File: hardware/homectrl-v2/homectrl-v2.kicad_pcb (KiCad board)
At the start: 4 copper layers, 64 x 70.5 mm, 127 parts, among them J1 Barrel_Jack, J2 PUMP1_CONN, J3 PUMP2_CONN, J4 STEP_CONN, J5 USB_C_CONN, J6 SMS1_CONN, J7 ALS_CONN, J8 FSW1_CONN, Q1 AO3407A, Q2 2N7002, Q3 AO3400A, Q4 AO3400A, SW1 S3_RESET_SW, SW2 S3_BOOT_SW, U1 TPS5405DR, U2 MCP1826S, U3 DMP4065S-7, U4 ESP32-S3-WROOM-1, U5 TMC2209, U7 TPD4E001DRLR, U8 TPD2E001DRLR, U9 SI2347DS-T1-GE3

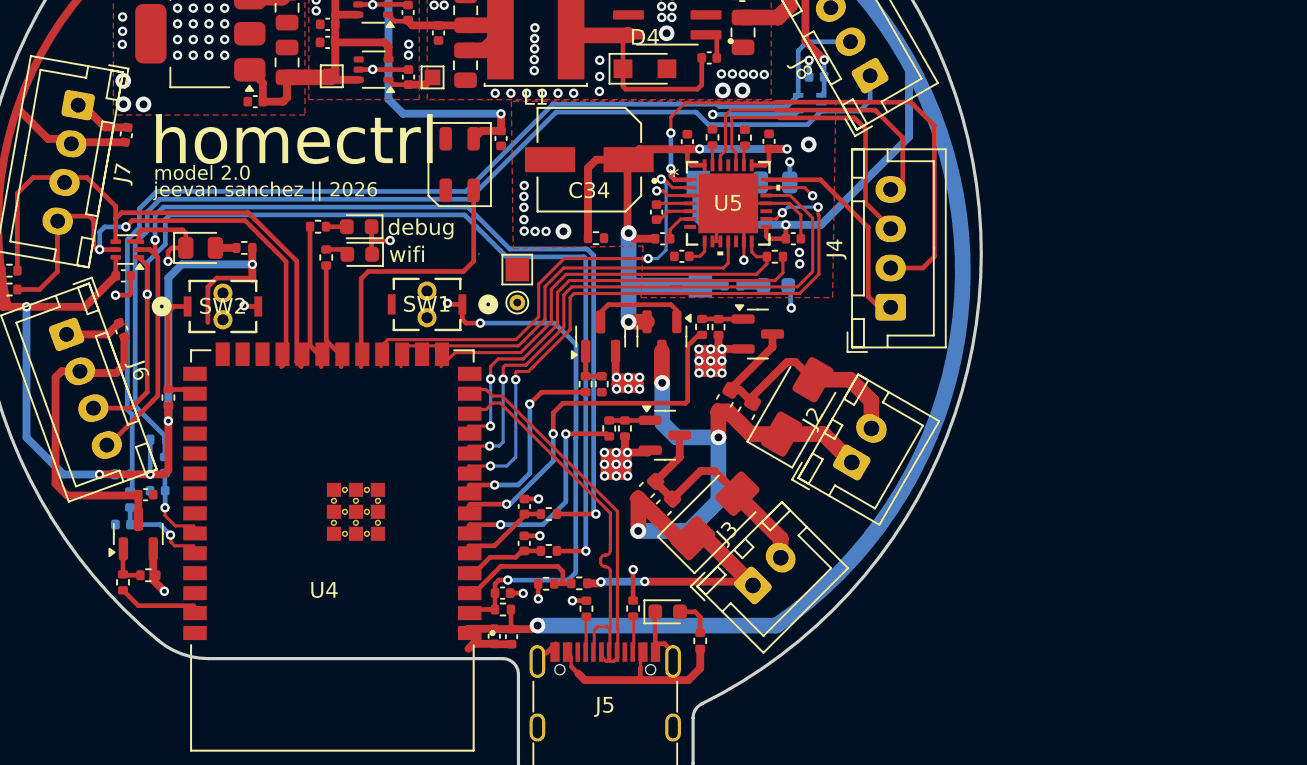
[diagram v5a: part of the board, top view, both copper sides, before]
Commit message: reroute esp pins
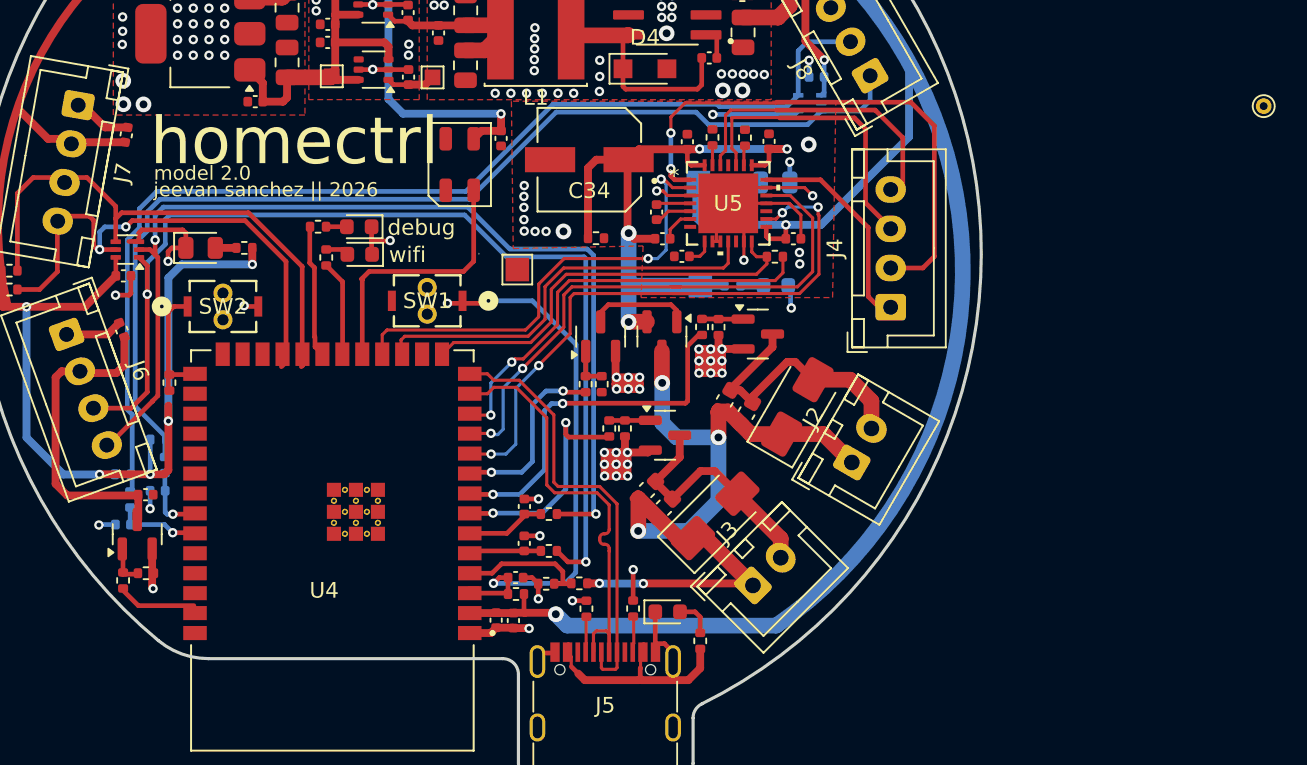
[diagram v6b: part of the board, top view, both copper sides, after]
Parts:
- moved TP3 49.2 mm to (175.5, 57.4)
- moved R9 1.29 mm to (127.9, 88.5)
- moved C17 1.29 mm to (127.8, 87.5)
- moved C16 1.03 mm to (127.7, 90.2)
- moved C14 1.03 mm to (126.6, 90.2)
- moved R14 0.95 mm to (105.8, 75.0)
- moved SW1 0.23 mm to (124.5, 69.8)
- moved R33 0.20 mm to (104.3, 87.2)
- moved R36 0.12 mm to (102.8, 87.7)
- moved Q1 0.07 mm to (103.7, 84.7)
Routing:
- net +3V3: track 198.5 -> 191.8 mm
- net USB_N: track 23.2 -> 28.2 mm
- net USB_P: track 24.1 -> 27.8 mm
- net GND: track 122.4 -> 125.7 mm, vias 152 -> 154
- net MTR_DIR: track 38.1 -> 36.5 mm
- net S3_EN: track 33.2 -> 34.7 mm
- net S3_RXD: track 28.7 -> 27.3 mm
- net MTR_STEP: track 40.9 -> 39.6 mm
- net Net-(J6-Pin_3): track 66.4 -> 67.4 mm
- net RGB_DATA: track 17.8 -> 16.9 mm
- net DBG_LED: track 9.22 -> 8.47 mm
- net WIFI_LED: track 6.84 -> 6.09 mm
- net SMS1_DATA: track 5.09 -> 4.38 mm
- net STEP_DIAG: track 26.8 -> 26.1 mm
- net VPMP_EN: track 17.4 -> 16.8 mm
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
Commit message: wrapping up layout & routing
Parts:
- removed the D8 at (107.8, 66.5)
- removed the R13 at (110.6, 66.5)
- removed TP13: 3V3_TP_DRILL, TestPoint:TestPoint_THTPad_D1.0mm_Drill0.5mm
- removed TP7: VBATT_TP_DRILL, TestPoint:TestPoint_THTPad_D1.0mm_Drill0.5mm
- added BZ1: CMT-0525-75-SMT-TR, CMT_0525_75_SMT_TR:XDCR_CMT-0525-75-SMT-TR, B.Cu at (118.8, 70.2)
- added C21: 0.1uF, Capacitor_SMD:C_0402_1005Metric, B.Cu at (113.2, 73.0)
- added D10: ON_LED, LED_SMD:LED_0603_1608Metric, F.Cu at (107.7, 66.4)
- added D13: BAT54J, Diode_SMD:D_SOD-323F, B.Cu at (115.1, 71.9)
- added Q5: AO3400A, Package_TO_SOT_SMD:SOT-23, B.Cu at (113.1, 68.3)
- added R15: 330, Resistor_SMD:R_0402_1005Metric, F.Cu at (110.5, 66.5)
- added R16: 200, Resistor_SMD:R_0402_1005Metric, B.Cu at (113.1, 71.8)
- added R19: 10k, Resistor_SMD:R_0402_1005Metric, B.Cu at (113.1, 70.8)
- added TP2: 3V3_TP_PAD, TestPoint:TestPoint_Pad_1.5x1.5mm, F.Cu at (108.4, 46.7)
- D2: footprint Diode_SMD:D_0603_1608Metric -> LED_SMD:LED_0603_1608Metric
- D7, R12: moved to F.Cu
- D8: footprint LED_SMD:LED_0805_2012Metric -> LED_SMD:LED_0603_1608Metric; moved to F.Cu
- R13: value 200 -> 330; moved to F.Cu
- TP5: value VBATT_TP_PAD -> TestPoint_Pad_D1.0mm; footprint TestPoint:TestPoint_Pad_1.5x1.5mm -> TestPoint:TestPoint_Pad_D1.0mm; moved to F.Cu
- moved TP3 47.8 mm to (128.8, 67.8), turned to 0 degrees
- moved D8 43.3 mm to (104.5, 45.4), turned to 0 degrees
- moved R13 38.8 mm to (106.6, 45.5), turned to -90 degrees
- moved D7 26.6 mm to (130.1, 46.4), turned to 0 degrees
- moved TP5 24.9 mm to (131.8, 45.2), turned to 0 degrees
- moved R12 24.1 mm to (132.9, 46.5), turned to 0 degrees
- moved R17 1.36 mm to (116.6, 64.9)
- moved D11 1.29 mm to (119.1, 64.9)
- moved D12 1.29 mm to (119.2, 66.6)
- moved R18 1.29 mm to (117.0, 66.8)
- moved TP1 1.23 mm to (126.7, 67.8), turned to 90 degrees
- moved U9 0.74 mm to (126.4, 43.6)
- moved D2 0.54 mm to (106.1, 32.6)
- moved R1 0.54 mm to (106.1, 35.4)
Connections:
- R12 pad 2: VPLUG -> Net-(R12-Pad2)
- R13 pad 1: +3V3 -> Net-(D8-A)
- R13 pad 2: Net-(D8-A) -> +3V3
- R36 pad 1: VPMP_EN -> VSMS_EN
- TP5 pad 1: VPLUG -> Net-(D3-K)
- U4 pad 24: unconnected-(U4-IO47-Pad24) -> BUZZ_EN
- U4 pad 26: BUZZ_EN -> unconnected-(U4-IO45-Pad26)
- U4 pad 38: VPMP_EN -> VSMS_EN
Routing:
- net 5V_USB: track 17.2 -> 67.8 mm, vias 0 -> 2
- net +3V3: track 191.8 -> 219.6 mm
- net GND: track 125.7 -> 142.7 mm, vias 154 -> 210
- net Net-(F1-Pad1): track 0.00 -> 13.3 mm
- net Net-(D13-A): track 0.00 -> 10.5 mm
- net VPLUG: track 57.2 -> 51.3 mm
- net VPMP_EN: track 16.8 -> 11.9 mm
- net VSMS_EN: track 0.00 -> 4.13 mm
- net Net-(Q5-G): track 0.00 -> 3.81 mm
- net Net-(D3-K): track 0.00 -> 2.68 mm
- net BUZZ_EN: track 0.00 -> 2.30 mm, vias 0 -> 1
- net Net-(D2-A): track 0.00 -> 1.47 mm
- net Net-(D8-A): track 2.68 -> 1.34 mm
- net Net-(D10-A): track 0.00 -> 1.34 mm
- net Net-(R12-Pad2): track 0.00 -> 1.22 mm
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- added copper zone on F.Cu, net Net-(D1-A2)
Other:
- board text added: "GND"
- board text added: "USB"
- board text added: "VCC"
- board text added: "VPLG"
- board text added: "on"

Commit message: reviewed
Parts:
- removed TP9: 3V3_TP_PAD, TestPoint:TestPoint_Pad_1.5x1.5mm
- added D15: VPMP_LED, LED_SMD:LED_0603_1608Metric, F.Cu at (147.0, 71.8)
- added R37: 1.8K, Resistor_SMD:R_0402_1005Metric, F.Cu at (146.4, 70.4)
- D11: value WIFI_LED -> DBG_LED
- D12: value DBG_LED -> WIFI_LED
- R10: value 680 -> 470
- R12: value 1K -> 1.8K
- R13, R15, R17: value 330 -> 150
- R16, R22, R24, R36, R7: value 200 -> 150
- R29, R30: footprint Resistor_SMD:R_0402_1005Metric -> Resistor_SMD:R_0603_1608Metric
- moved D3 1.88 mm to (129.6, 41.4)
- moved R30 0.83 mm to (142.7, 58.7)
- moved R29 0.80 mm to (140.4, 58.6)
- moved TP1 0.20 mm to (126.7, 68.0)
- moved TP3 0.20 mm to (128.8, 68.0)
- moved C35 0.06 mm to (138.8, 59.8)
- turned R16 to 180 degrees
- turned R17 to 180 degrees
- turned R18 to -90 degrees
- turned R22 to -90 degrees
- turned R24 to -90 degrees
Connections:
- R12 pad 2: Net-(R12-Pad2) -> Net-(D3-K)
- R16 pad 1: BUZZ_EN -> Net-(Q5-G)
- R16 pad 2: Net-(Q5-G) -> BUZZ_EN
- R17 pad 1: DBG_LED -> Net-(D11-A)
- R17 pad 2: Net-(D11-A) -> DBG_LED
- R18 pad 1: WIFI_LED -> Net-(D12-A)
- R18 pad 2: Net-(D12-A) -> WIFI_LED
- R22 pad 1: PUMP1_EN -> Net-(Q3-G)
- R22 pad 2: Net-(Q3-G) -> PUMP1_EN
- R24 pad 1: PUMP2_EN -> Net-(Q4-G)
- R24 pad 2: Net-(Q4-G) -> PUMP2_EN
- U7 pad 1: Net-(J6-Pin_4) -> Net-(J6-Pin_3)
- U7 pad 2: Net-(J6-Pin_3) -> Net-(J6-Pin_4)
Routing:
- net VPLUG: track 51.3 -> 71.4 mm, vias 4 -> 6
- net VPMP: track 52.6 -> 66.3 mm, vias 4 -> 5
- net +3V3: track 219.6 -> 211.2 mm
- net GND: track 142.7 -> 149.9 mm, vias 210 -> 215
- net Net-(Q2-D): track 6.53 -> 12.5 mm, vias 0 -> 2
- net Net-(D15-A): track 0.00 -> 1.98 mm
- net PUMP2_EN: track 15.1 -> 13.5 mm
- net STEP_1A: track 19.7 -> 21.4 mm
- net STEP_1B: track 18.8 -> 20.2 mm
- net Net-(D3-K): track 2.68 -> 3.90 mm
- net Net-(R12-Pad2): track 1.22 -> 0.00 mm
- net Net-(U5-BRB): track 1.26 -> 2.25 mm
- net S3_BOOT: track 7.91 -> 6.99 mm
- added copper zone on In1.Cu, net GND
- added copper zone on In2.Cu, net GND
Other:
- outline, holes or cut-outs redrawn
- board text added: "VP"
